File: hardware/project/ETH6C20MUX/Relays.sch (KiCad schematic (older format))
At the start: 82 parts, among them J301 5499141-4, K301 HE3621A0510, K302 HE3621A0510, K303 HE3621A0510, K304 HE3621A0510, K305 HE3621A0510, K306 HE3621A0510, K307 HE3621A0510, K308 HE3621A0510, K309 HE3621A0510, K310 HE3621A0510, K311 HE3621A0510, K312 HE3621A0510, K313 HE3621A0510, K314 HE3621A0510, K315 HE3621A0510, K316 HE3621A0510, K317 HE3621A0510, K318 HE3621A0510, K319 HE3621A0510, K320 HE3621A0510, K321 HE3621A0510, K322 HE3621A0510, K323 HE3621A0510, K324 HE3621A0510, K325 HE3621A0510, K326 HE3621A0510, K327 HE3621A0510, K328 HE3621A0510, K329 HE3621A0510, K330 HE3621A0510, K331 HE3621A0510, K332 HE3621A0510, K333 HE3621A0510, K334 HE3621A0510, K335 HE3621A0510, K336 HE3621A0510, K337 HE3621A0510, K338 HE3621A0510, K339 HE3621A0510, K340 HE3621A0510, K341 HE3621A0510, K342 HE3621A0510, K343 HE3621A0510, K344 HE3621A0510, K345 HE3621A0510, K346 HE3621A0510, K347 HE3621A0510, K348 HE3621A0510, K349 HE3621A0510, K350 HE3621A0510, K351 HE3621A0510, K352 HE3621A0510, K353 HE3621A0510, K354 HE3621A0510, K355 HE3621A0510, K356 HE3621A0510, K357 HE3621A0510, K358 HE3621A0510, K359 HE3621A0510, K360 HE3621A0510, K361 HE3621A0510, K362 HE3621A0510, K363 HE3621A0510, K364 HE3621A0510, K365 HE3621A0510, K366 HE3621A0510, U301 MCZ33996, U302 MCZ33996, U303 MCZ33996, U304 MCZ33996, U305 MCZ33996

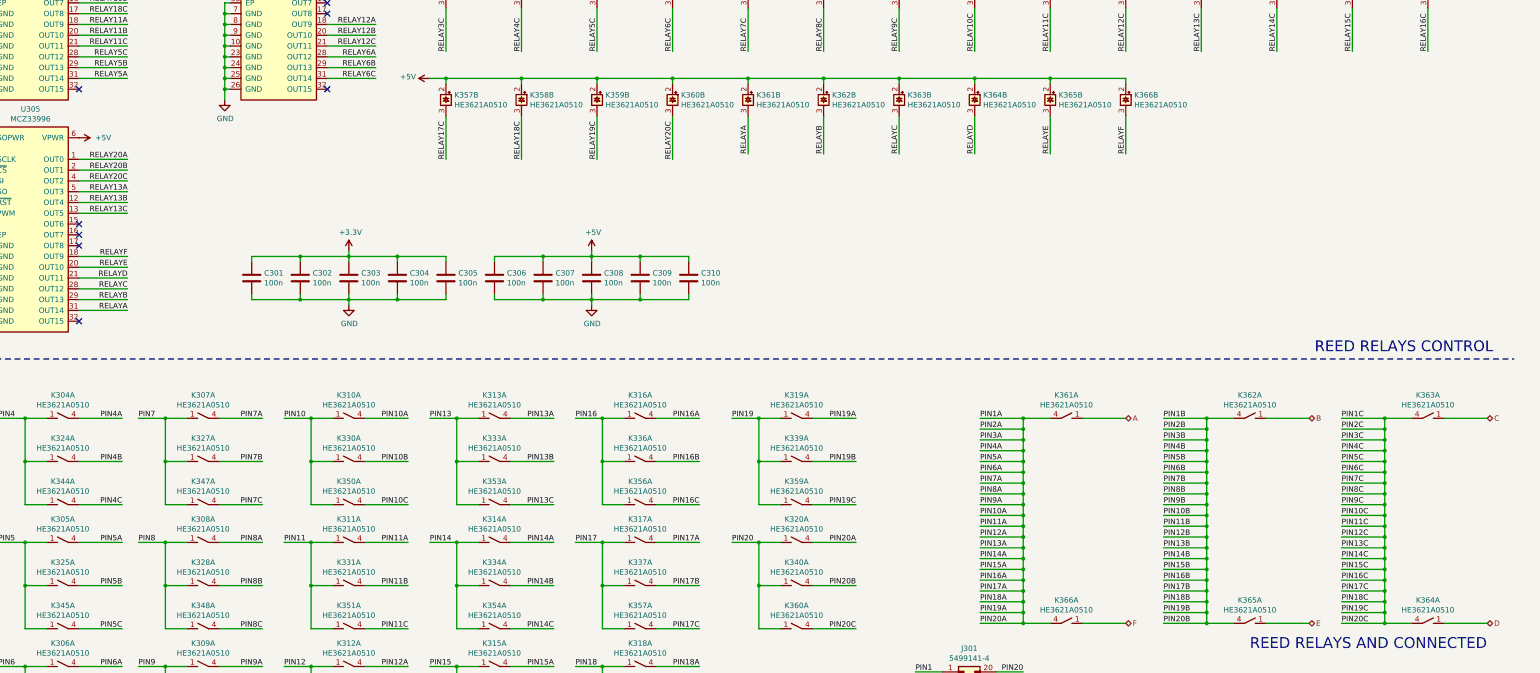
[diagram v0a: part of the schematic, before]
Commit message: Added pin swap for A,B,E and F.
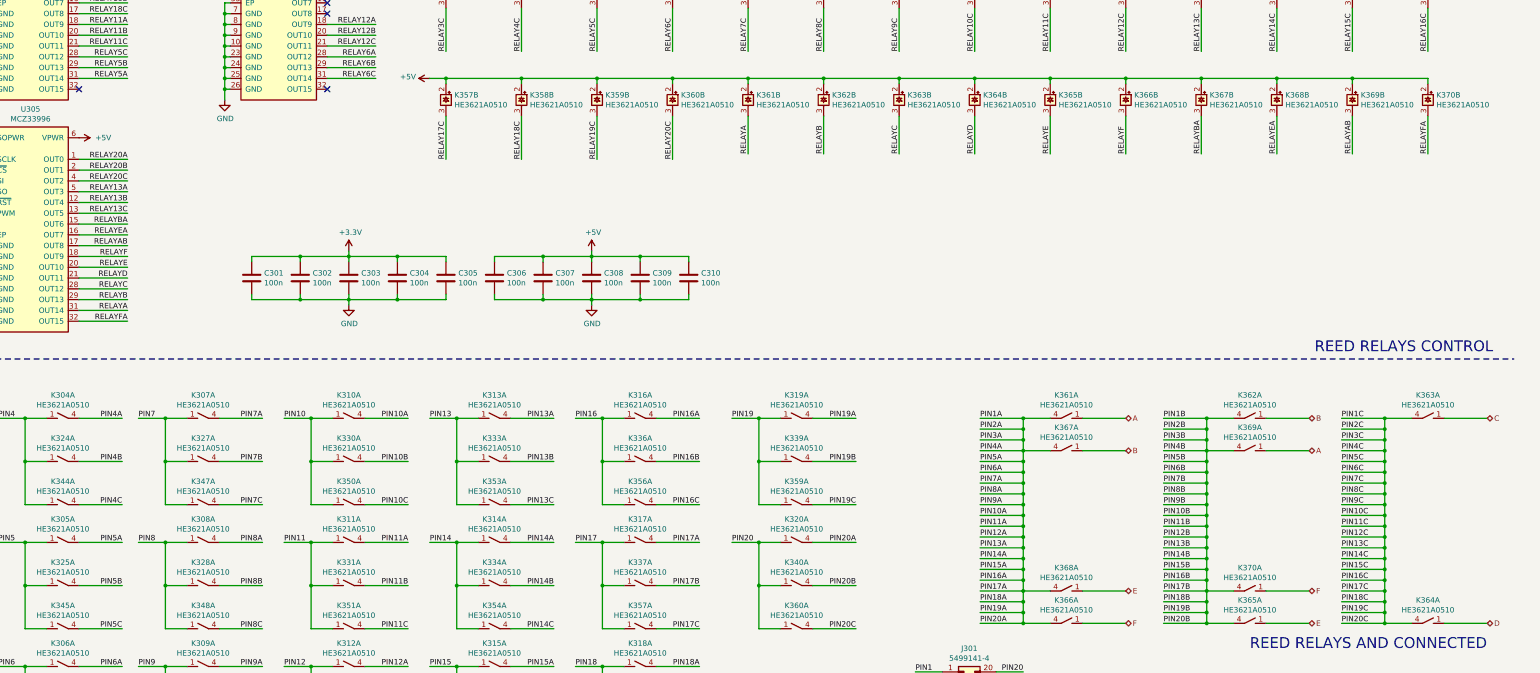
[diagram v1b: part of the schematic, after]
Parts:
- added K367, K368, K369, K370: HE3621A0510, ETH6C20MUX:HE360_x-5050462-8, symbol ETH6C20MUX:HE3600
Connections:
- net +5V: now also K367.2, K368.2, K369.2, K370.2
- net A: now also K369.1
- net B: now also K367.1
- net E: now also K368.1
- net F: now also K370.1
- net PIN10A: now also K367.4, K368.4
- net PIN10B: now also K369.4, K370.4
- net RELAYBA: now reaches U305.15 (OUT6)
- net RELAYBA: now also K367.3
- net RELAYEA: now reaches U305.16 (OUT7)
- net RELAYEA: now also K368.3
- net RELAYAB: now reaches U305.17 (OUT8)
- net RELAYAB: now also K369.3
- net RELAYFA: now reaches U305.32 (OUT15)
- net RELAYFA: now also K370.3
- no-connect marks 19 -> 15
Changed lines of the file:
@@
 Wire Wire Line
 	1750 5450 1800 5450
-NoConn ~ 2700 6850
 Wire Wire Line
 	3700 8550 3500 8550
@@
 NoConn ~ 5000 3900
 NoConn ~ 5000 4000
-NoConn ~ 2700 6150
-NoConn ~ 2700 6050
-NoConn ~ 2700 5950
 $Comp
 L Device:C C301
@@
 $EndComp
 NoConn ~ 5000 4700
+$Comp
+L ETH6C20MUX:HE3600 K367
+U 1 1 5EB2648E
+P 11850 8050
+F 0 "K367" V 12065 8050 50  0000 C CNN
+F 1 "HE3621A0510" V 11974 8050 50  0000 C CNN
+F 2 "ETH6C20MUX:HE360_x-5050462-8" H 12100 8000 50  0001 C CNN
+F 3 "" H 12100 8000 50  0001 C CNN
+	1    11850 8050
+	0    1    -1   0
+$EndComp
+$Comp
+L ETH6C20MUX:HE3600 K367
+U 2 1 5EB27C7F
+P 13100 4800
+F 0 "K367" H 13178 4846 50  0000 L CNN
+F 1 "HE3621A0510" H 13178 4755 50  0000 L CNN
+F 2 "ETH6C20MUX:HE360_x-5050462-8" H 13350 4750 50  0001 C CNN
+F 3 "" H 13350 4750 50  0001 C CNN
+	2    13100 4800
+	1    0    0    -1
+$EndComp
+$Comp
+L ETH6C20MUX:HE3600 K368
+U 1 1 5EB2BCD2
+P 11850 9350
+F 0 "K368" V 12065 9350 50  0000 C CNN
+F 1 "HE3621A0510" V 11974 9350 50  0000 C CNN
+F 2 "ETH6C20MUX:HE360_x-5050462-8" H 12100 9300 50  0001 C CNN
+F 3 "" H 12100 9300 50  0001 C CNN
+	1    11850 9350
+	0    1    -1   0
+$EndComp
+$Comp
+L ETH6C20MUX:HE3600 K368
+U 2 1 5EB2BCD8
+P 13800 4800
+F 0 "K368" H 13878 4846 50  0000 L CNN
+F 1 "HE3621A0510" H 13878 4755 50  0000 L CNN
+F 2 "ETH6C20MUX:HE360_x-5050462-8" H 14050 4750 50  0001 C CNN
+F 3 "" H 14050 4750 50  0001 C CNN
+	2    13800 4800
+	1    0    0    -1
+$EndComp
+$Comp
+L ETH6C20MUX:HE3600 K369
+U 1 1 5EBCC795
+P 13550 8050
+F 0 "K369" V 13765 8050 50  0000 C CNN
+F 1 "HE3621A0510" V 13674 8050 50  0000 C CNN
+F 2 "ETH6C20MUX:HE360_x-5050462-8" H 13800 8000 50  0001 C CNN
+F 3 "" H 13800 8000 50  0001 C CNN
+	1    13550 8050
+	0    1    -1   0
+$EndComp
+$Comp
+L ETH6C20MUX:HE3600 K369
+U 2 1 5EBCC79B
+P 14500 4800
+F 0 "K369" H 14578 4846 50  0000 L CNN
+F 1 "HE3621A0510" H 14578 4755 50  0000 L CNN
+F 2 "ETH6C20MUX:HE360_x-5050462-8" H 14750 4750 50  0001 C CNN
+F 3 "" H 14750 4750 50  0001 C CNN
+	2    14500 4800
+	1    0    0    -1
+$EndComp
+$Comp
+L ETH6C20MUX:HE3600 K370
+U 1 1 5EC6D994
+P 13550 9350
+F 0 "K370" V 13765 9350 50  0000 C CNN
+F 1 "HE3621A0510" V 13674 9350 50  0000 C CNN
+F 2 "ETH6C20MUX:HE360_x-5050462-8" H 13800 9300 50  0001 C CNN
+F 3 "" H 13800 9300 50  0001 C CNN
+	1    13550 9350
+	0    1    -1   0
+$EndComp
+$Comp
+L ETH6C20MUX:HE3600 K370
+U 2 1 5EC6D99A
+P 15200 4800
+F 0 "K370" H 15278 4846 50  0000 L CNN
+F 1 "HE3621A0510" H 15278 4755 50  0000 L CNN
+F 2 "ETH6C20MUX:HE360_x-5050462-8" H 15450 4750 50  0001 C CNN
+F 3 "" H 15450 4750 50  0001 C CNN
+	2    15200 4800
+	1    0    0    -1
+$EndComp
+Wire Wire Line
+	11700 8050 11450 8050
+Text HLabel 12400 8050 2    50   BiDi ~ 0
+B
+Wire Wire Line
+	12400 8050 12000 8050
+Wire Wire Line
+	11700 9350 11450 9350
+Wire Wire Line
+	12000 9350 12400 9350
+Text HLabel 12400 9350 2    50   BiDi ~ 0
+E
+Wire Wire Line
+	13700 8050 14100 8050
+Text HLabel 14100 8050 2    50   BiDi ~ 0
+A
+Wire Wire Line
+	13700 9350 14100 9350
+Text HLabel 14100 9350 2    50   BiDi ~ 0
+F
+Wire Wire Line
+	13400 8050 13150 8050
+Wire Wire Line
+	12400 4600 13100 4600
+Wire Wire Line
+	15200 4600 15200 4650
+Connection ~ 12400 4600
+Wire Wire Line
+	14500 4650 14500 4600
+Connection ~ 14500 4600
+Wire Wire Line
+	14500 4600 15200 4600
+Wire Wire Line
+	13800 4650 13800 4600
+Connection ~ 13800 4600
+Wire Wire Line
+	13800 4600 14500 4600
+Wire Wire Line
+	13100 4650 13100 4600
+Connection ~ 13100 4600
+Wire Wire Line
+	13100 4600 13800 4600
+Text Label 13100 5300 1    50   ~ 0
+RELAYBA
+Wire Wire Line
+	13100 4950 13100 5300
+Text Label 13800 5300 1    50   ~ 0
+RELAYEA
+Wire Wire Line
+	13800 4950 13800 5300
+Text Label 14500 5300 1    50   ~ 0
+RELAYAB
+Wire Wire Line
+	14500 4950 14500 5300
+Text Label 15200 5300 1    50   ~ 0
+RELAYFA
+Wire Wire Line
+	15200 4950 15200 5300
+Wire Wire Line
+	13150 9350 13400 9350
+Text Label 3150 5950 2    50   ~ 0
+RELAYBA
+Wire Wire Line
+	2700 5950 3150 5950
+Text Label 3150 6050 2    50   ~ 0
+RELAYEA
+Wire Wire Line
+	2700 6050 3150 6050
+Text Label 3150 6150 2    50   ~ 0
+RELAYAB
+Wire Wire Line
+	2700 6150 3150 6150
+Text Label 3150 6850 2    50   ~ 0
+RELAYFA
+Wire Wire Line
+	2700 6850 3150 6850
 $EndSCHEMATC

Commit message: PCB redesign
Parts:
- C301, C302, C303, C304, C305, C306, C307, C308, C309, C310: footprint Capacitor_SMD:C_0603_1608Metric_Pad1.05x0.95mm_HandSolder -> Capacitor_SMD:C_0603_1608Metric_Pad1.08x0.95mm_HandSolder
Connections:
- net RELAY14A: now also U305.1 (OUT0); no longer U301.4 (OUT2)
- net RELAY14B: now also U305.2 (OUT1); no longer U301.5 (OUT3)
- net RELAY14C: now also U301.15 (OUT6); no longer U301.12 (OUT4)
- net RELAY1B: now also U301.13 (OUT5); no longer U301.16 (OUT7)
- net RELAY1C: now also U301.32 (OUT15); no longer U301.17 (OUT8)
- net RELAY20A: now also U301.4 (OUT2); no longer U305.1 (OUT0)
- net RELAY20B: now also U301.5 (OUT3); no longer U305.2 (OUT1)
- net RELAY7B: now also U301.12 (OUT4); no longer U301.13 (OUT5)
- net RELAY7C: now also U301.31 (OUT14); no longer U301.15 (OUT6)
- net RELAY8B: now also U301.17 (OUT8); no longer U301.29 (OUT13)
- net RELAY8C: now also U301.16 (OUT7); no longer U301.31 (OUT14)
- no-connect marks 15 -> 14
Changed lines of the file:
@@
 	5000 1250 5450 1250
 Wire Wire Line
-	2700 1450 3150 1450
+	2700 1650 3150 1650
 Wire Wire Line
 	2700 5850 3150 5850
@@
 Text Label 5450 1250 2    50   ~ 0
 RELAY16C
-Text Label 3150 1450 2    50   ~ 0
+Text Label 3150 1650 2    50   ~ 0
 RELAY14C
 Text Label 3150 5850 2    50   ~ 0
@@
 	5000 1150 5450 1150
 Wire Wire Line
-	2700 1350 3150 1350
+	2700 5450 3150 5450
 Wire Wire Line
 	2700 5750 3150 5750
@@
 	5000 1450 5450 1450
 Wire Wire Line
-	2700 1750 3150 1750
+	2700 1550 3150 1550
 Wire Wire Line
 	5000 1650 5450 1650
@@
 	5000 4500 5450 4500
 Wire Wire Line
-	2700 1550 3150 1550
-Wire Wire Line
-	2700 2350 3150 2350
+	2700 1450 3150 1450
+Wire Wire Line
+	2700 1850 3150 1850
 Text Label 5450 1150 2    50   ~ 0
 RELAY16B
-Text Label 3150 1350 2    50   ~ 0
+Text Label 3150 5450 2    50   ~ 0
 RELAY14B
 Text Label 3150 5750 2    50   ~ 0
@@
 Text Label 5450 1450 2    50   ~ 0
 RELAY9B
-Text Label 3150 2350 2    50   ~ 0
+Text Label 3150 1850 2    50   ~ 0
 RELAY8B
-Text Label 3150 1550 2    50   ~ 0
+Text Label 3150 1450 2    50   ~ 0
 RELAY7B
 Text Label 5450 4500 2    50   ~ 0
@@
 Text Label 5450 1650 2    50   ~ 0
 RELAY2B
+Text Label 3150 1550 2    50   ~ 0
+RELAY1B
+Wire Wire Line
+	2700 3200 3150 3200
+Wire Wire Line
+	2700 4400 3150 4400
+Wire Wire Line
+	5000 4600 5450 4600
+Wire Wire Line
+	2700 2450 3150 2450
+Wire Wire Line
+	2700 1750 3150 1750
 Text Label 3150 1750 2    50   ~ 0
-RELAY1B
-Wire Wire Line
-	2700 3200 3150 3200
-Wire Wire Line
-	2700 4400 3150 4400
-Wire Wire Line
-	5000 4600 5450 4600
-Wire Wire Line
-	2700 1650 3150 1650
-Wire Wire Line
-	2700 2450 3150 2450
+RELAY8C
 Text Label 3150 2450 2    50   ~ 0
-RELAY8C
-Text Label 3150 1650 2    50   ~ 0
 RELAY7C
 Text Label 5450 4600 2    50   ~ 0
@@
 	5000 1050 5450 1050
 Wire Wire Line
-	2700 1250 3150 1250
+	2700 5350 3150 5350
 Wire Wire Line
 	2700 5650 3150 5650
@@
 Text Label 5450 1050 2    50   ~ 0
 RELAY16A
-Text Label 3150 1250 2    50   ~ 0
+Text Label 3150 5350 2    50   ~ 0
 RELAY14A
 Text Label 3150 5650 2    50   ~ 0
@@
 Wire Wire Line
 	8200 4950 8200 5350
-Text Label 3150 1850 2    50   ~ 0
+Text Label 3150 2550 2    50   ~ 0
 RELAY1C
 Text Label 5450 1850 2    50   ~ 0
@@
 	5000 1850 5450 1850
 Wire Wire Line
-	2700 1850 3150 1850
-NoConn ~ 2700 2550
+	2700 2550 3150 2550
 NoConn ~ 5000 2550
 NoConn ~ 2700 4700
@@
 RELAY20C
 Wire Wire Line
-	2700 5450 3150 5450
-Text Label 3150 5450 2    50   ~ 0
+	2700 1350 3150 1350
+Text Label 3150 1350 2    50   ~ 0
 RELAY20B
 Wire Wire Line
-	2700 5350 3150 5350
-Text Label 3150 5350 2    50   ~ 0
+	2700 1250 3150 1250
+Text Label 3150 1250 2    50   ~ 0
 RELAY20A
 Wire Wire Line
@@
 F 0 "C301" H 4415 6496 50  0000 L CNN
 F 1 "100n" H 4415 6405 50  0000 L CNN
-F 2 "Capacitor_SMD:C_0603_1608Metric_Pad1.05x0.95mm_HandSolder" H 4338 6300 50  0001 C CNN
+F 2 "Capacitor_SMD:C_0603_1608Metric_Pad1.08x0.95mm_HandSolder" H 4338 6300 50  0001 C CNN
 F 3 "~" H 4300 6450 50  0001 C CNN
 	1    4300 6450
@@
 F 0 "C302" H 4865 6496 50  0000 L CNN
 F 1 "100n" H 4865 6405 50  0000 L CNN
-F 2 "Capacitor_SMD:C_0603_1608Metric_Pad1.05x0.95mm_HandSolder" H 4788 6300 50  0001 C CNN
+F 2 "Capacitor_SMD:C_0603_1608Metric_Pad1.08x0.95mm_HandSolder" H 4788 6300 50  0001 C CNN
 F 3 "~" H 4750 6450 50  0001 C CNN
 	1    4750 6450
@@
 F 0 "C303" H 5315 6496 50  0000 L CNN
 F 1 "100n" H 5315 6405 50  0000 L CNN
-F 2 "Capacitor_SMD:C_0603_1608Metric_Pad1.05x0.95mm_HandSolder" H 5238 6300 50  0001 C CNN
+F 2 "Capacitor_SMD:C_0603_1608Metric_Pad1.08x0.95mm_HandSolder" H 5238 6300 50  0001 C CNN
 F 3 "~" H 5200 6450 50  0001 C CNN
 	1    5200 6450
@@
 F 0 "C304" H 5765 6496 50  0000 L CNN
 F 1 "100n" H 5765 6405 50  0000 L CNN
-F 2 "Capacitor_SMD:C_0603_1608Metric_Pad1.05x0.95mm_HandSolder" H 5688 6300 50  0001 C CNN
+F 2 "Capacitor_SMD:C_0603_1608Metric_Pad1.08x0.95mm_HandSolder" H 5688 6300 50  0001 C CNN
 F 3 "~" H 5650 6450 50  0001 C CNN
 	1    5650 6450
@@
 F 0 "C305" H 6215 6496 50  0000 L CNN
 F 1 "100n" H 6215 6405 50  0000 L CNN
-F 2 "Capacitor_SMD:C_0603_1608Metric_Pad1.05x0.95mm_HandSolder" H 6138 6300 50  0001 C CNN
+F 2 "Capacitor_SMD:C_0603_1608Metric_Pad1.08x0.95mm_HandSolder" H 6138 6300 50  0001 C CNN
 F 3 "~" H 6100 6450 50  0001 C CNN
 	1    6100 6450
@@
 F 0 "C306" H 6665 6496 50  0000 L CNN
 F 1 "100n" H 6665 6405 50  0000 L CNN
-F 2 "Capacitor_SMD:C_0603_1608Metric_Pad1.05x0.95mm_HandSolder" H 6588 6300 50  0001 C CNN
+F 2 "Capacitor_SMD:C_0603_1608Metric_Pad1.08x0.95mm_HandSolder" H 6588 6300 50  0001 C CNN
 F 3 "~" H 6550 6450 50  0001 C CNN
 	1    6550 6450
@@
 F 0 "C307" H 7115 6496 50  0000 L CNN
 F 1 "100n" H 7115 6405 50  0000 L CNN
-F 2 "Capacitor_SMD:C_0603_1608Metric_Pad1.05x0.95mm_HandSolder" H 7038 6300 50  0001 C CNN
+F 2 "Capacitor_SMD:C_0603_1608Metric_Pad1.08x0.95mm_HandSolder" H 7038 6300 50  0001 C CNN
 F 3 "~" H 7000 6450 50  0001 C CNN
 	1    7000 6450
@@
 F 0 "C308" H 7565 6496 50  0000 L CNN
 F 1 "100n" H 7565 6405 50  0000 L CNN
-F 2 "Capacitor_SMD:C_0603_1608Metric_Pad1.05x0.95mm_HandSolder" H 7488 6300 50  0001 C CNN
+F 2 "Capacitor_SMD:C_0603_1608Metric_Pad1.08x0.95mm_HandSolder" H 7488 6300 50  0001 C CNN
 F 3 "~" H 7450 6450 50  0001 C CNN
 	1    7450 6450
@@
 F 0 "C309" H 8015 6496 50  0000 L CNN
 F 1 "100n" H 8015 6405 50  0000 L CNN
-F 2 "Capacitor_SMD:C_0603_1608Metric_Pad1.05x0.95mm_HandSolder" H 7938 6300 50  0001 C CNN
+F 2 "Capacitor_SMD:C_0603_1608Metric_Pad1.08x0.95mm_HandSolder" H 7938 6300 50  0001 C CNN
 F 3 "~" H 7900 6450 50  0001 C CNN
 	1    7900 6450
@@
 F 0 "C310" H 8465 6496 50  0000 L CNN
 F 1 "100n" H 8465 6405 50  0000 L CNN
-F 2 "Capacitor_SMD:C_0603_1608Metric_Pad1.05x0.95mm_HandSolder" H 8388 6300 50  0001 C CNN
+F 2 "Capacitor_SMD:C_0603_1608Metric_Pad1.08x0.95mm_HandSolder" H 8388 6300 50  0001 C CNN
 F 3 "~" H 8350 6450 50  0001 C CNN
 	1    8350 6450
